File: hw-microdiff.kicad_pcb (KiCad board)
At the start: 2 copper layers, 44 x 50 mm, 30 parts, among them J1 RJ45, J2 JST 1x8, J3 Screw_Terminal_01x02, SW1 SW_DIP_x02, U1 5V, U2 RS-485 IC, U3 3.3V

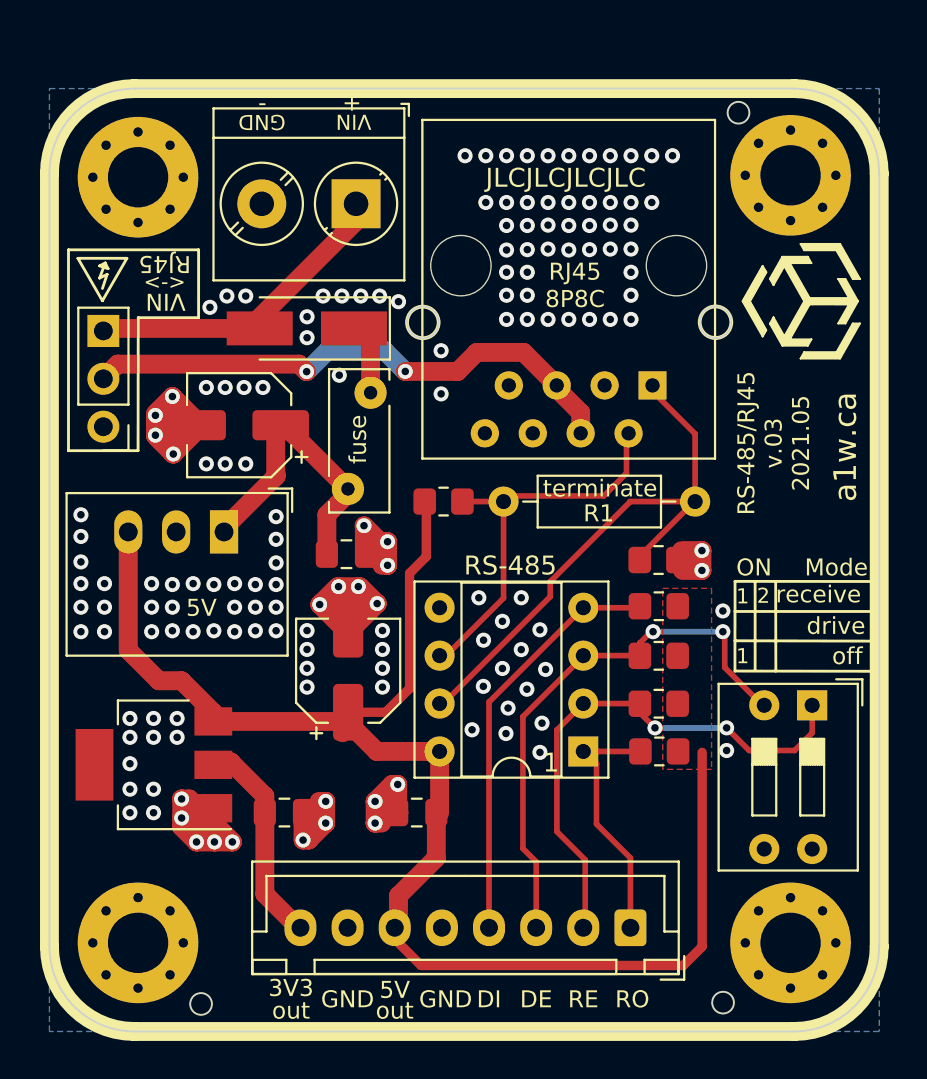
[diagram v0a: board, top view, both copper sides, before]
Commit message: Finish PCB routing for v.04
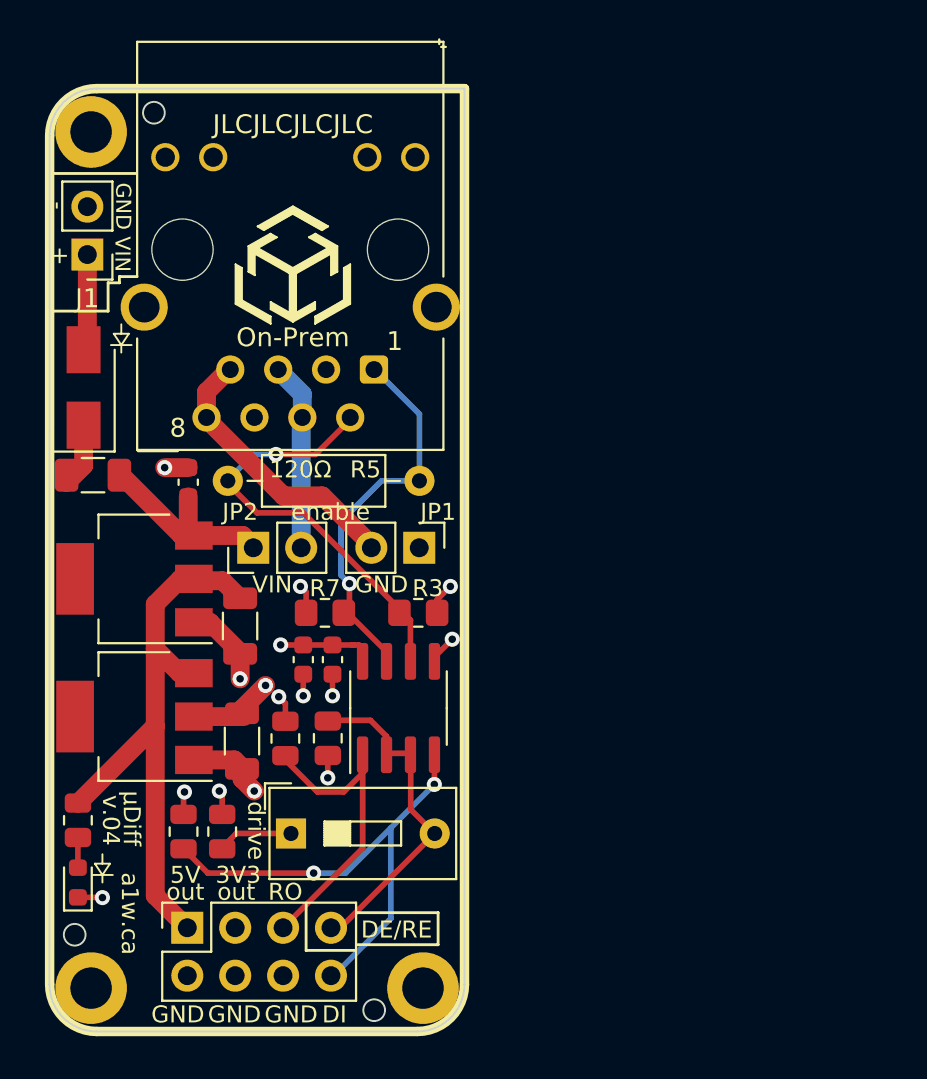
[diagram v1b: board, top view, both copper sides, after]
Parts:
- removed H1: M3_MountingHole_Pad, MountingHole:MountingHole_3.2mm_M3_Pad_Via
- removed SW1: SW_DIP_x02, Button_Switch_THT:SW_DIP_SPSTx02_Slide_9.78x7.26mm_W7.62mm_P2.54mm
- added D2: Blue LED, LED_SMD:LED_0603_1608Metric, F.Cu at (41.5, 142.1)
- added JP2: enable, Connector_PinHeader_2.54mm:PinHeader_1x02_P2.54mm_Vertical, F.Cu at (50.8, 124.3)
- added JP3: drive EN, Button_Switch_THT:SW_DIP_SPSTx01_Slide_9.78x4.72mm_W7.62mm_P2.54mm, F.Cu at (52.8, 139.5)
- added R8: 10K, Resistor_SMD:R_0805_2012Metric, F.Cu at (47.1, 139.4)
- added REF**: led_direction, hw-microdiff:led_direction, F.Cu at (43.8, 113.6)
- added REF**: led_direction, hw-microdiff:led_direction, F.Cu at (42.8, 141.7)
- C1: value 0.1uF -> 0.1uF 50V; footprint Capacitor_SMD:C_0805_2012Metric_Pad1.18x1.45mm_HandSolder -> Capacitor_SMD:C_0603_1608Metric
- C2: value 10uF -> 22uF 10V; footprint Capacitor_SMD:CP_Elec_5x5.3 -> Capacitor_SMD:C_1206_3216Metric
- C3: value 22uF -> 22uF 10V; footprint Capacitor_SMD:CP_Elec_5x5.3 -> Capacitor_SMD:C_1206_3216Metric
- C4: value 10uF -> 0.1uF 50V; footprint Capacitor_SMD:C_0805_2012Metric_Pad1.18x1.45mm_HandSolder -> Capacitor_SMD:C_0603_1608Metric
- C5: value 10uF -> 10uF 10V; footprint Capacitor_SMD:C_0805_2012Metric_Pad1.18x1.45mm_HandSolder -> Capacitor_SMD:C_0603_1608Metric
- D1: value D_Schottky -> Diode 40V/3A; footprint Diode_SMD:D_SMA_Handsoldering -> Diode_SMD:D_SMA
- F1: value Polyfuse -> Fuse 24V/1A; footprint Fuse:Fuse_Bourns_MF-RHT050 -> Fuse:Fuse_1206_3216Metric
- H2, H3, H4: value M3_MountingHole_Pad -> M2_MountingHole; footprint MountingHole:MountingHole_3.2mm_M3_Pad_Via -> MountingHole:MountingHole_2.2mm_M2_ISO14580_Pad
- J1: value RJ45 -> Power Input; footprint Connector_RJ:RJ45_Amphenol_54602-x08_Horizontal -> Connector_PinHeader_2.54mm:PinHeader_1x02_P2.54mm_Vertical
- J2: value JST 1x8 -> Header 2x4P; footprint Connector_JST:JST_XH_B8B-XH-A_1x08_P2.50mm_Vertical -> Connector_PinSocket_2.54mm:PinSocket_2x04_P2.54mm_Vertical
- J3: value Screw_Terminal_01x02 -> 8P8C; footprint TerminalBlock_Phoenix:TerminalBlock_Phoenix_PT-1,5-2-5.0-H_1x02_P5.00mm_Horizontal -> Connector_RJ:RJ45_Hanrun_HR911105A
- JP1: value JUMPER -> GND EN; footprint Connector_PinHeader_2.54mm:PinHeader_1x03_P2.54mm_Vertical -> Connector_PinHeader_2.54mm:PinHeader_1x02_P2.54mm_Vertical
- R1: value 120R -> 220R; footprint Resistor_THT:R_Axial_DIN0207_L6.3mm_D2.5mm_P10.16mm_Horizontal -> Resistor_SMD:R_0805_2012Metric
- R2, R4: footprint Resistor_SMD:R_0805_2012Metric_Pad1.20x1.40mm_HandSolder -> Resistor_SMD:R_0805_2012Metric
- R3: value 10K -> 20K
- R5: value 10K -> 120R; footprint Resistor_SMD:R_0805_2012Metric_Pad1.20x1.40mm_HandSolder -> Resistor_THT:R_Axial_DIN0207_L6.3mm_D2.5mm_P10.16mm_Horizontal
- R6: value 20K -> 10K; footprint Resistor_SMD:R_0805_2012Metric_Pad1.20x1.40mm_HandSolder -> Resistor_SMD:R_0805_2012Metric
- U1: value 5V -> 5V/1A; footprint Converter_DCDC:Converter_DCDC_RECOM_R-78E-0.5_THT -> Package_TO_SOT_SMD:SOT-223
- U2: value RS-485 IC -> 3.3V/1A; footprint Package_DIP:DIP-8_W7.62mm_Socket -> Package_TO_SOT_SMD:SOT-223
- U3: value 3.3V -> RS-485; footprint Package_TO_SOT_SMD:SOT-223 -> Package_SO:SOIC-8_3.9x4.9mm_P1.27mm
- moved R1 36.8 mm to (41.5, 138.8), turned to 270 degrees
- moved REF** 36.4 mm to (43.4, 124.7)
- moved J1 30.8 mm to (42.0, 108.8)
- moved G*** 27.9 mm to (52.1, 108.6)
- moved G*** 27.1 mm to (52.9, 109.4), turned to 0 degrees
- moved R5 27.0 mm to (49.5, 120.8)
- moved R4 24.1 mm to (49.2, 139.4), turned to 90 degrees
- moved U2 23.9 mm to (44.5, 133.3)
- moved J2 23.5 mm to (47.3, 144.5), turned to 90 degrees
- moved R2 21.0 mm to (52.5, 134.5), turned to 90 degrees
- moved JP1 20.3 mm to (59.6, 124.3), turned to 270 degrees
- moved R6 19.9 mm to (54.8, 134.4), turned to 270 degrees
- moved H3 19.6 mm to (59.8, 147.7)
- moved F1 15.4 mm to (42.3, 120.5), turned to 0 degrees
- moved U3 13.3 mm to (58.5, 132.8), turned to 90 degrees
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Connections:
- net /PWR renamed Net-(D1-Pad1)
- C1 pad 1: FUSE -> /VIN
- C2 pad 1: FUSE -> +5V
- C3 pad 1: +5V -> GND
- C3 pad 2: GND -> +3V3
- C4 pad 1: GND -> +3V3
- C4 pad 2: +3V3 -> GND
- C5 pad 1: +5V -> +3V3
- D1 pad 2: VIN -> Net-(D1-Pad2)
- F1 pad 2: FUSE -> /VIN
- H2 pad 1: GND -> (no net)
- H3 pad 1: GND -> (no net)
- H4 pad 1: GND -> (no net)
- J1 pad 1: B -> Net-(D1-Pad2)
- J1 pad 2: A -> GND
- J2 pad 1: RO -> +5V
- J2 pad 2: RE -> GND
- J2 pad 3: DE -> +3V3
- J2 pad 4: DI -> GND
- J2 pad 5: GND -> /RO
- J2 pad 6: +5V -> GND
- J2 pad 7: GND -> /DE_RE
- J2 pad 8: +3V3 -> /DI
- J3 pad 1: VIN -> /b1
- J3 pad 2: GND -> /a1
- JP1 pad 1: VIN -> GND
- JP1 pad 2: /VDD -> /VSS
- R1 pad 1: B -> +5V
- R1 pad 2: A -> Net-(D2-Pad2)
- R2 pad 1: DI -> /RO
- R2 pad 2: +5V -> +3V3
- R3 pad 1: DE -> /a1
- R3 pad 2: +5V -> +3V3
- R4 pad 1: RE -> Net-(JP3-Pad1)
- R4 pad 2: +5V -> +3V3
- R5 pad 1: RO -> /a1
- R5 pad 2: +5V -> /b1
- R6 pad 1: B -> /DE_RE
- R7 pad 1: A -> /b1
- R7 pad 2: +5V -> GND
- U1 pad 1: FUSE -> GND
- U1 pad 2: GND -> +5V
- U1 pad 3: +5V -> /VIN
- U2 pad 1: RO -> GND
- U2 pad 2: RE -> +3V3
- U2 pad 3: DE -> +5V
- U2 pad 4: DI -> (no net)
- U3 pad 1: GND -> /RO
- U3 pad 2: +3V3 -> /DE_RE
- U3 pad 3: +5V -> /DE_RE
- U3 pad 4: (no net) -> /DI
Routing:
- net GND: track 77.8 -> 19.4 mm, vias 158 -> 10
- net +5V: track 78.1 -> 31.7 mm
- net B: track 30.1 -> 0.00 mm
- net DE: track 29.4 -> 0.00 mm, vias 2 -> 0
- net RE: track 28.6 -> 0.00 mm, vias 2 -> 0
- net /DI: track 0.00 -> 26.7 mm, vias 0 -> 2
- net /a1: track 0.00 -> 23.1 mm, vias 0 -> 1
- net DI: track 22.1 -> 0.00 mm
- net A: track 21.3 -> 0.00 mm
- net /b1: track 0.00 -> 20.3 mm, vias 0 -> 1
- net /VDD: track 29.2 -> 9.82 mm, vias 2 -> 0
- net /DE_RE: track 0.00 -> 18.1 mm
- net VIN: track 17.1 -> 0.00 mm
- net /RO: track 0.00 -> 16.4 mm
- net FUSE: track 15.6 -> 0.00 mm
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- added copper zone on In1.Cu, net +3V3
- added copper zone on In2.Cu, net GND
- removed copper zone on F.Cu, net +5V
- removed copper zone on B.Cu, net GND
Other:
- board size 44 x 50 mm -> 22 x 50 mm
- copper layers 2 -> 4
- board text added: "120Ω"
- board text added: "DE/RE"
- board text added: "On-Prem"
- board text added: "RS485 μDiff 2022.07.v04 o-p.jp/5e1"
- board text added: "enable"
- board text added: "v.04"
- board text added: "μDiff"
- board text removed: "2"
- board text removed: "<->"
- board text removed: "DE"
- board text removed: "Mode"
- board text removed: "ON"
- board text removed: "RE"
- board text removed: "RJ45"
- board text removed: "RJ45 8P8C"
- board text removed: "RS-485"
- board text removed: "RS-485/RJ45 v.03 2021.05"
- board text removed: "caution!"
- board text removed: "fuse"
- board text removed: "high voltage high current"
- board text removed: "off"
- board text removed: "terminate"

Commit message: Minor layout corrections:   - Add test pads on back of PCB   - Remove 10K pullup   - Adjust silkscreens   - Update to KiCad 6.0   - Add 3D model for RJ45 connector   - Add VDD pin for unprotected VIN   - Add open jumpers and remove DIP switch   - Connect RJ45 shield and H2 mounting hole to Earth, not ground
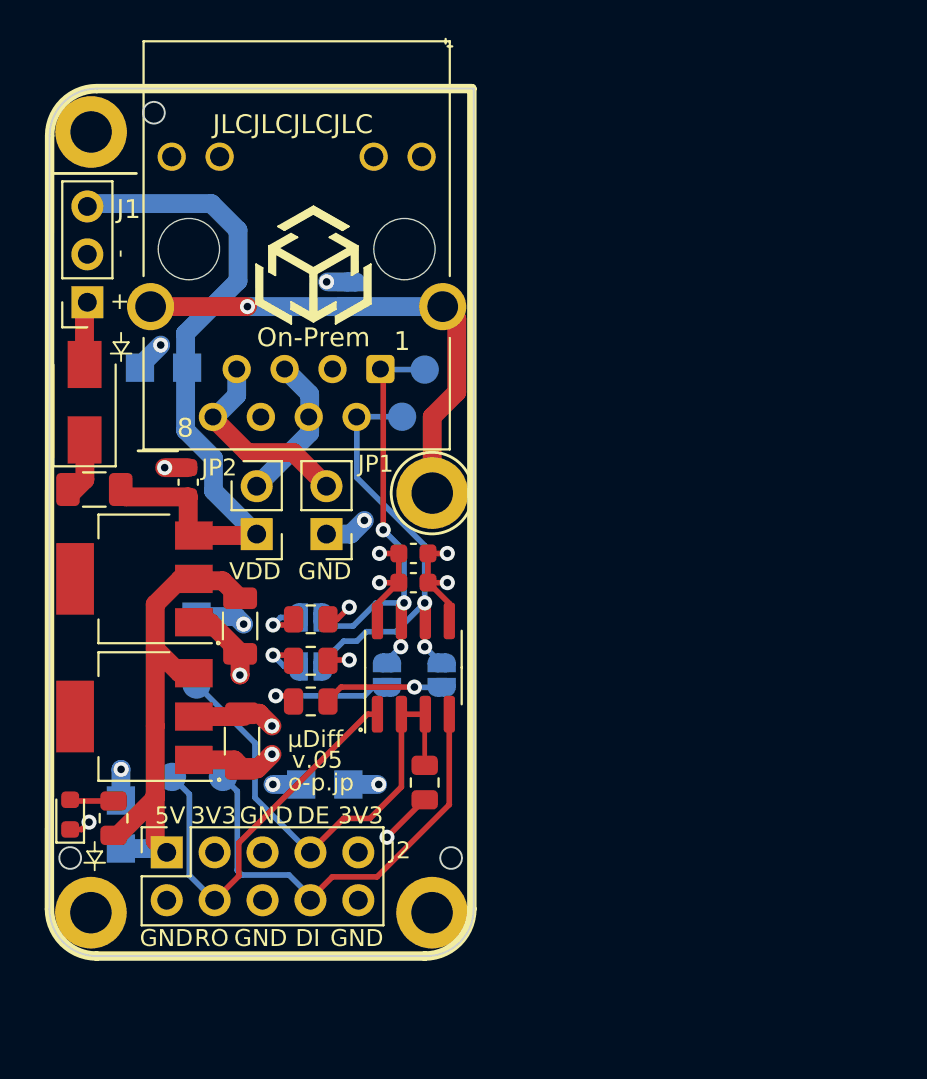
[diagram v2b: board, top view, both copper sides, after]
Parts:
- removed the R2 at (52.5, 134.5)
- removed the R4 at (49.2, 139.4)
- removed R8: 10K, Resistor_SMD:R_0805_2012Metric
- removed the REF** at (43.5, 134.4)
- added H2: M2_MountingHole, MountingHole:MountingHole_2.2mm_M2_ISO14580_Pad, F.Cu at (60.3, 121.5)
- added JP4: Biasing-, Jumper:SolderJumper-2_P1.3mm_Open_RoundedPad1.0x1.5mm, B.Cu at (53.9, 128.0)
- added JP5: Biasing+, Jumper:SolderJumper-2_P1.3mm_Open_RoundedPad1.0x1.5mm, B.Cu at (53.9, 130.6)
- added JP6: Terminating, Jumper:SolderJumper-2_P1.3mm_Open_RoundedPad1.0x1.5mm, B.Cu at (60.8, 131.1)
- added JP7: Terminating, Jumper:SolderJumper-2_P1.3mm_Open_RoundedPad1.0x1.5mm, B.Cu at (57.9, 131.1)
- added OSHW_Mono_0.1_Scale: JP000009, hw-microdiff:OSHW_Mono_0.1_Scale, B.Cu at (52.0, 110.3)
- added TP4: TP_GND, TestPoint:TestPoint_Pad_1.5x1.5mm, B.Cu at (43.8, 137.8)
- added TP6: TP_GND, TestPoint:TestPoint_Pad_1.5x1.5mm, B.Cu at (55.9, 136.9)
- added locked: TP_VDD, TestPoint:TestPoint_Pad_1.5x1.5mm, B.Cu at (47.3, 114.8)
- added locked: TP_B1, TestPoint:TestPoint_Pad_D1.5mm, B.Cu at (59.9, 114.9)
- added locked: TP_GND, TestPoint:TestPoint_Pad_1.5x1.5mm, B.Cu at (44.8, 114.8)
- added locked: TP_5V, TestPoint:TestPoint_Pad_1.5x1.5mm, B.Cu at (43.8, 140.3)
- added locked: TP_3V3, TestPoint:TestPoint_Pad_1.5x1.5mm, B.Cu at (53.4, 136.9)
- added locked: TP_RO, TestPoint:TestPoint_Pad_D1.5mm, B.Cu at (46.5, 136.5)
- added locked: TP_DI, TestPoint:TestPoint_Pad_D1.5mm, B.Cu at (49.2, 136.5)
- added locked: TP_DE_RE, TestPoint:TestPoint_Pad_D1.5mm, B.Cu at (47.8, 131.6)
- added locked: TP_GND, TestPoint:TestPoint_Pad_1.5x1.5mm, B.Cu at (47.8, 128.0)
- added locked: TP_A1, TestPoint:TestPoint_Pad_D1.5mm, B.Cu at (58.7, 117.4)
- J1: footprint Connector_PinHeader_2.54mm:PinHeader_1x02_P2.54mm_Vertical -> Connector_PinSocket_2.54mm:PinSocket_1x03_P2.54mm_Vertical
- J2: value Header 2x4P -> Header 2x5P; footprint Connector_PinSocket_2.54mm:PinSocket_2x04_P2.54mm_Vertical -> Connector_PinSocket_2.54mm:PinSocket_2x05_P2.54mm_Vertical
- JP2: value enable -> VIN EN
- JP3: value drive EN -> Grounding; footprint Button_Switch_THT:SW_DIP_SPSTx01_Slide_9.78x4.72mm_W7.62mm_P2.54mm -> Jumper:SolderJumper-2_P1.3mm_Open_RoundedPad1.0x1.5mm; moved to B.Cu
- R3: value 20K -> 390R; footprint Resistor_SMD:R_0805_2012Metric_Pad1.20x1.40mm_HandSolder -> Resistor_SMD:R_0805_2012Metric
- R4: renamed from R7; value 20K -> 390R; footprint Resistor_SMD:R_0805_2012Metric_Pad1.20x1.40mm_HandSolder -> Resistor_SMD:R_0805_2012Metric
- R5: value 120R -> 100R; footprint Resistor_THT:R_Axial_DIN0207_L6.3mm_D2.5mm_P10.16mm_Horizontal -> Resistor_SMD:R_0805_2012Metric
- moved JP3 28.8 mm to (56.0, 110.9), turned to 90 degrees
- moved REF** 23.2 mm to (53.1, 103.6)
- moved G*** 17.0 mm to (43.6, 123.3)
- moved R5 12.5 mm to (53.9, 132.5), turned to 180 degrees
- moved C5 7.12 mm to (59.3, 126.2), turned to 0 degrees
- moved C4 7.08 mm to (59.3, 124.7), turned to 0 degrees
- moved R3 6.24 mm to (53.9, 130.3)
- moved R2 5.65 mm to (59.9, 136.8)
- moved JP1 4.97 mm to (54.7, 123.6), turned to 180 degrees
- moved J2 4.15 mm to (46.2, 140.5)
- moved H3 4.03 mm to (60.3, 143.7)
- moved H4 4.00 mm to (42.2, 143.7)
- moved D2 3.62 mm to (41.1, 138.5)
- moved J1 2.53 mm to (42.0, 111.3)
- moved U3 2.29 mm to (59.3, 130.7)
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- renumbered H2 to H1, R6 to R2
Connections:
- net /VSS renamed Net-(J3-Pad7)
- C1 pad 1: /VIN -> /VDD
- D1 pad 2: Net-(D1-Pad2) -> /VIN
- F1 pad 2: /VIN -> /VDD
- J1 pad 1: Net-(D1-Pad2) -> /VIN
- J2 pad 4: GND -> /RO
- J2 pad 5: /RO -> GND
- J3 pad 1: /b1 -> /A-
- J3 pad 2: /a1 -> /A+
- J3 pad 3: Net-(J3-Pad3) -> unconnected-(J3-Pad3)
- J3 pad 4: /VDD -> Net-(J3-Pad4)
- J3 pad 5: /VDD -> Net-(J3-Pad4)
- J3 pad 6: Net-(J3-Pad6) -> unconnected-(J3-Pad6)
- J3 pad SH: GND -> Earth
- JP2 pad 1: /VIN -> /VDD
- JP2 pad 2: /VDD -> Net-(J3-Pad4)
- JP3 pad 1: Net-(JP3-Pad1) -> Earth
- JP3 pad 2: /DE_RE -> GND
- R3 pad 1: /a1 -> /A1+
- R4 pad 1: /b1 -> /A1-
- R5 pad 1: /a1 -> /A2+
- R5 pad 2: /b1 -> /A2-
- U1 pad 3: /VIN -> /VDD
- U3 pad 6: /a1 -> /A+
- U3 pad 7: /b1 -> /A-
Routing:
- net /VDD: track 9.82 -> 36.8 mm
- net Earth: track 0.00 -> 26.3 mm, vias 0 -> 1
- net /A+: track 0.00 -> 24.2 mm, vias 0 -> 2
- net /A-: track 0.00 -> 23.9 mm, vias 0 -> 3
- net /a1: track 23.1 -> 0.00 mm, vias 1 -> 0
- net /b1: track 20.3 -> 0.00 mm, vias 1 -> 0
- net GND: track 19.4 -> 32.6 mm, vias 10 -> 14
- net Net-(J3-Pad4): track 0.00 -> 7.86 mm
- net /DE_RE: track 18.1 -> 25.4 mm
- net /VIN: track 10.7 -> 3.46 mm
- net /A2-: track 0.00 -> 7.19 mm, vias 0 -> 1
- net /A2+: track 0.00 -> 6.42 mm, vias 0 -> 1
- net Net-(D1-Pad2): track 5.00 -> 0.00 mm
- net /RO: track 16.4 -> 21.2 mm
- net +5V: track 31.7 -> 27.2 mm
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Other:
- board size 22 x 50 mm -> 22.5 x 46 mm
- net class Default removed
- board text added: "DE"
- board text added: "RS485 μDiff 2022.09.v05"
- board text added: "VDD"
- board text added: "VDD unprotected"
- board text added: "biasing"
- board text added: "o-p.jp"
- board text added: "o-p.jp/f6a"
- board text added: "term"
- board text added: "v.05"
- board text removed: "120Ω"
- board text removed: "DE/RE"
- board text removed: "RS485 μDiff 2022.07.v04 o-p.jp/5e1"
- board text removed: "a1w.ca"
- board text removed: "drive"
- board text removed: "out"
- board text removed: "receive"
- board text removed: "v.04"
